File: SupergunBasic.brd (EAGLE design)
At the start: 114.9 x 67.3 mm, 33 parts, among them J1 AUDIO_JACK_3.5MM_PTH

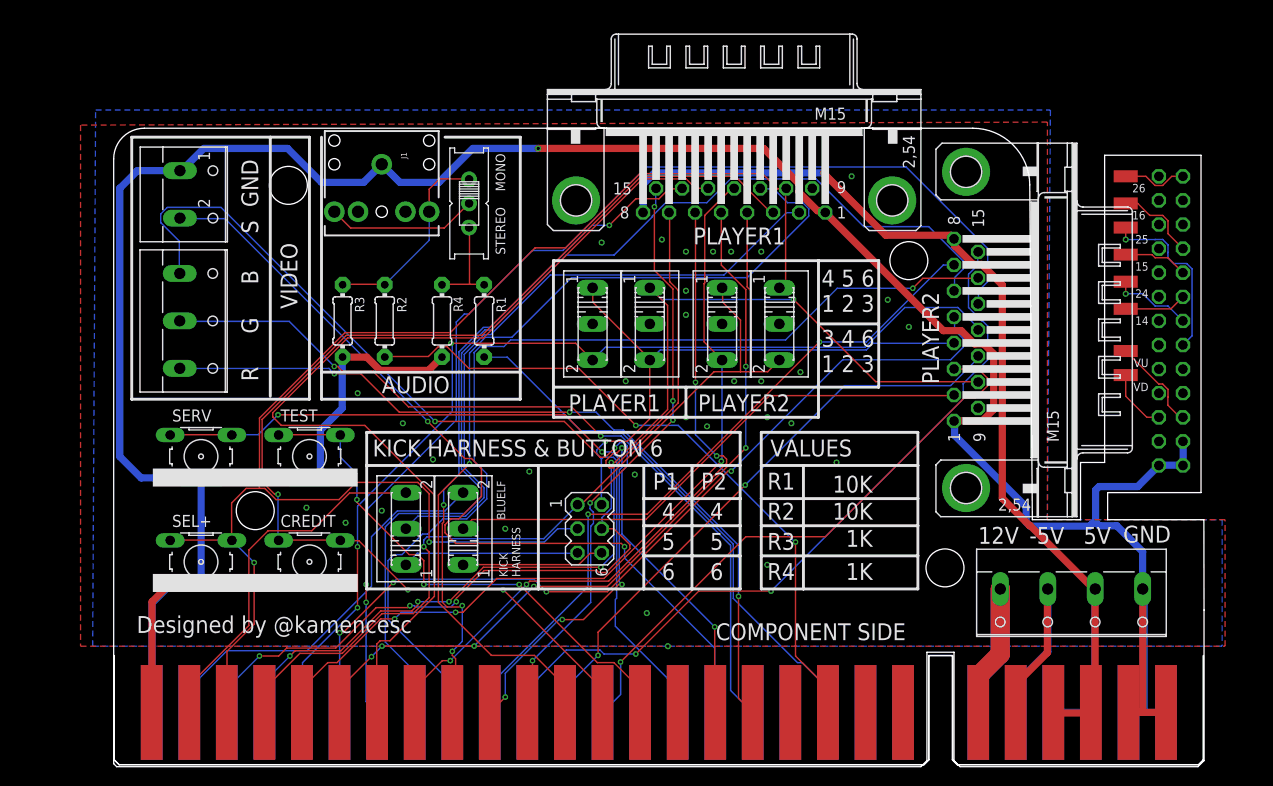
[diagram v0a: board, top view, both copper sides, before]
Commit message: Add files via upload
He estado trabajando en la versión con Scart, es mas fácil quitar que añadir cosas, así que en el momento de subir esta versión, es identica a la Scart pero sin los requisitos de este.
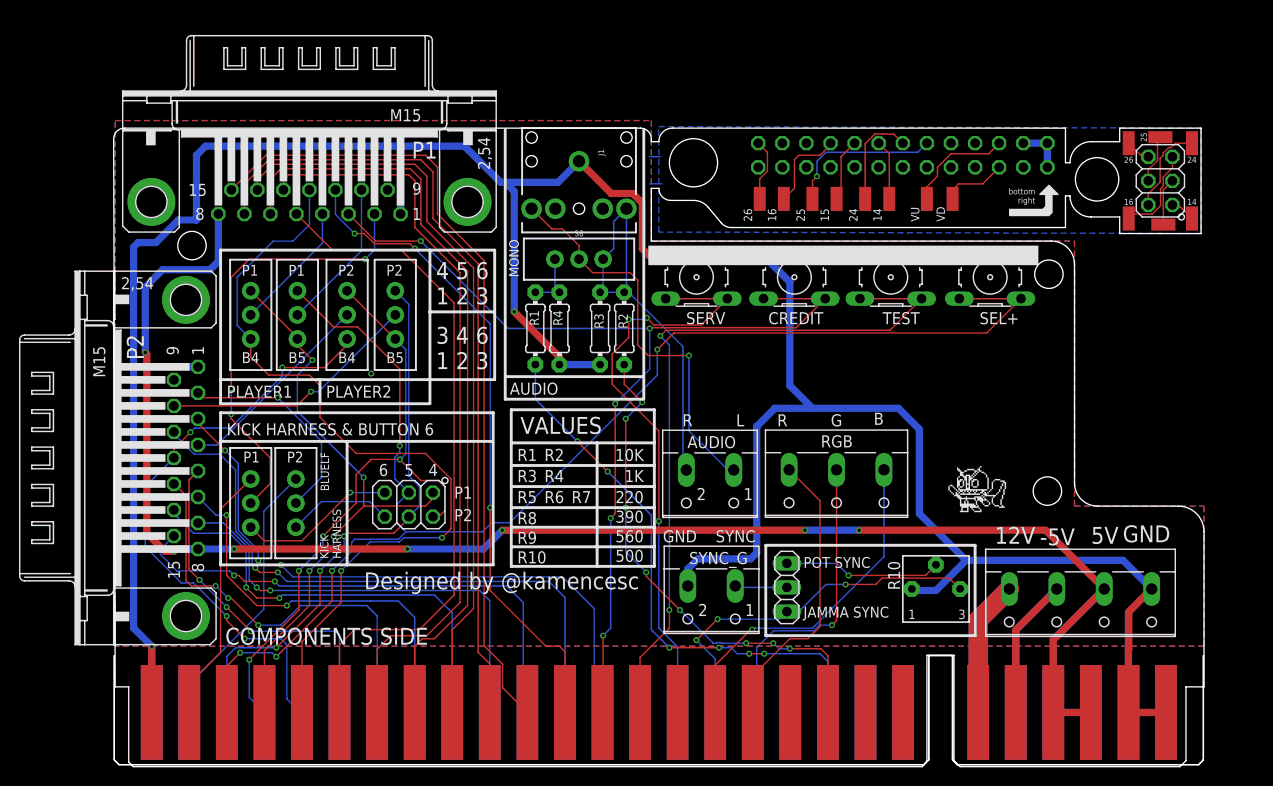
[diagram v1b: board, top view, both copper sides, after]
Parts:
- removed KH_CPS2: (no value), con-lstb:MA03-2
- removed MO_ST: (no value), adafruit:EG1218
- removed S2, S3, S5, S6: (no value), switch:255SB
- removed X4: (no value), con-wago-500:W237-102
- removed X5: (no value), con-wago-500:W237-103
- added 1, 2, 3, 4, 5, 6: (no value), wirepad:SMD1,27-2,54
- added AUDIO, SYNC_G: (no value), con-wago-500:W237-102
- added JP2, JP3: (no value), pinhead:2X03
- added JP4: (no value), pinhead:1X03
- added R10: (no value), bourns:3362P
- added RGB: (no value), con-wago-500:W237-103
- added S10, S11, S12, S8, S9: (no value), SparkFun-Switches:SWITCH_SPDT_PTH_11.6X4.0MM
- R1, R2: value (none) -> 10K
- R3, R4: value (none) -> 1K
- S1, S4: device switch:255SB -> SparkFun-Switches:SWITCH_SPDT_PTH_11.6X4.0MM
- moved SEL+ 88.4 mm to (92.4, 51.6), turned to 180 degrees
- moved PLAYER_2 83.3 mm to (7.62, 32.5), turned to 270 degrees
- moved TEST 64.1 mm to (81.9, 51.6), turned to 180 degrees
- moved CREDIT 59.3 mm to (71.8, 51.6), turned to 180 degrees
- moved SERV 55.5 mm to (61.4, 51.6), turned to 180 degrees
- moved S4 54.3 mm to (19.2, 27.8), turned to 180 degrees
- moved S1 53.2 mm to (14.4, 27.8), turned to 180 degrees
- moved PLAYER_1 44.8 mm to (20.6, 59.5)
- moved 26 38.6 mm to (68.1, 59.8), turned to 0 degrees
- moved 16 36.0 mm to (70.6, 59.8), turned to 0 degrees
- moved JP1 33.2 mm to (83.2, 64.5), turned to 180 degrees
- moved 25 33.2 mm to (73.7, 59.8), turned to 0 degrees
- moved 15 31.0 mm to (76.2, 59.8), turned to 0 degrees
- moved 24 28.8 mm to (79.2, 59.8), turned to 0 degrees
- moved 14 27.5 mm to (81.8, 59.8), turned to 0 degrees
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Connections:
- removed net N$11: JAMMA1.11
- removed net N$3: MO_ST.S, R1.1, R4.2
- removed net N$5: JAMMA2.M
- removed net P1_B6: PLAYER_1.2, S2.2
- removed net P2_B6: PLAYER_2.2, S3.2
- new net DIRECT_SYNC: JP4.2, SYNC_G.1
- new net K_14: 1.1, JP2.1
- new net K_15: 2.1, JP2.3
- new net K_16: 3.1, JP2.5
- new net K_24: 6.1, JP2.2
- new net K_25: 5.1, JP2.4
- new net K_26: 4.1, JP2.6
- new net P_SYNC: JP4.3, R10.2
- new net STR_LEFT: R1.1, R4.2, S8.3
- new net SW1_B6: PLAYER_1.2, S1.2
- new net SW2_B6: PLAYER_2.2, S4.2
- net AUDIO_LEFT: now also AUDIO.1, S8.2; no longer MO_ST.P
- net AUDIO_RIGHT: now also AUDIO.2, S8.1; no longer MO_ST.O
- net GND: now also R10.1, SYNC_G.2; no longer X4.1
- net J_BLUE: now also RGB.1; no longer X5.1
- net J_GREEN: now also RGB.2; no longer X5.2
- net J_P1_B6: now also S1.3; no longer S2.3
- net J_P2_B6: now also S4.3; no longer S3.3
- net J_RED: now also RGB.3; no longer X5.3
- net J_SYNC: now also JP4.1, R10.3; no longer X4.2
- net K_P1_B6: now also JP3.5, S1.1; no longer KH_CPS2.5, S2.1
- net K_P2_B6: now also JP3.6, S4.1; no longer KH_CPS2.6, S3.1
- net P1_B3: now also S9.3; no longer S1.3
- net P1_B4: now also JP3.1, S12.3, S9.1; no longer KH_CPS2.1, PLAYER_1.4, S1.1, S4.3
- net P1_B5: now also JP3.3, S12.1; no longer KH_CPS2.3, PLAYER_1.10, S4.1
- net P2_B3: now also S11.3; no longer S5.3
- net P2_B4: now also JP3.2, S10.3, S11.1; no longer KH_CPS2.2, PLAYER_2.4, S5.1, S6.3
- net P2_B5: now also JP3.4, S10.1; no longer KH_CPS2.4, PLAYER_2.10, S6.1
- net SW1_B4: now also PLAYER_1.4, S9.2; no longer S1.2
- net SW1_B5: now also PLAYER_1.10, S12.2; no longer S4.2
- net SW2_B4: now also PLAYER_2.4, S11.2; no longer S5.2
- net SW2_B5: now also PLAYER_2.10, S10.2; no longer S6.2
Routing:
- net P2_B1: track 118.2 -> 44.3 mm, vias 2 -> 3
- net P2_RIGHT: track 116.0 -> 42.2 mm, vias 0 -> 2
- net P1_B6: track 67.1 -> 0.00 mm
- net VCC: track 117.1 -> 183.4 mm, vias 1 -> 7
- net P2_B5: track 123.7 -> 59.3 mm, vias 5 -> 3
- net J_BLUE: track 100.7 -> 36.7 mm, vias 3 -> 1
- net P2_B6: track 57.6 -> 0.00 mm
- net P2_LEFT: track 104.3 -> 47.1 mm, vias 1 -> 2
- net J_GREEN: track 86.5 -> 32.5 mm, vias 2 -> 1
- net J_RED: track 84.9 -> 31.0 mm, vias 3 -> 0
- net P2_B2: track 91.3 -> 37.6 mm, vias 4 -> 3
- net P2_B4: track 119.8 -> 66.3 mm, vias 5 -> 4
- net J_SYNC: track 92.6 -> 39.4 mm, vias 2 -> 3
- net SW1_B6: track 0.00 -> 46.5 mm, vias 0 -> 3
- net P2_B3: track 105.3 -> 62.9 mm, vias 3 -> 4
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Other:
- outline, holes or cut-outs redrawn
- board text added: "14"
- board text added: "15"
- board text added: "16"
- board text added: "220"
- board text added: "24"
- board text added: "25"
- board text added: "26"
- board text added: "390"
- board text added: "500"
- board text added: "560"
- board text added: "B"
- board text added: "B4"
- board text added: "B5"
- board text added: "Basic Supergun + Scart V0.2"
- board text added: "COMPONENTS SIDE"
- board text added: "Faces to the PCB"
- board text added: "G"
- board text added: "JAMMA SYNC"
- board text added: "L"
- board text added: "POT SYNC"
- board text added: "R"
- board text added: "R10"
- board text added: "R5"
- board text added: "R6"
- board text added: "R7"
- board text added: "R8"
- board text added: "R9"
- board text added: "SYNC"
- board text added: "bottom right"
- board text removed: "Basic Supergun"
- board text removed: "COMPONENT SIDE"
- board text removed: "R G B"
- board text removed: "S GND"
- board text removed: "STEREO"
- board text removed: "VIDEO"

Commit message: Add files via upload
There ara some changesr since las versión, now there's a lm1881 sync stripper to get Sync On Green to Scart Connector. But if you are using a OSSC theres a switch to select Jamma Sync (original) or Csync (LM1881)

Now there's a LED to bring light to the PCB!

Minir improvements on design
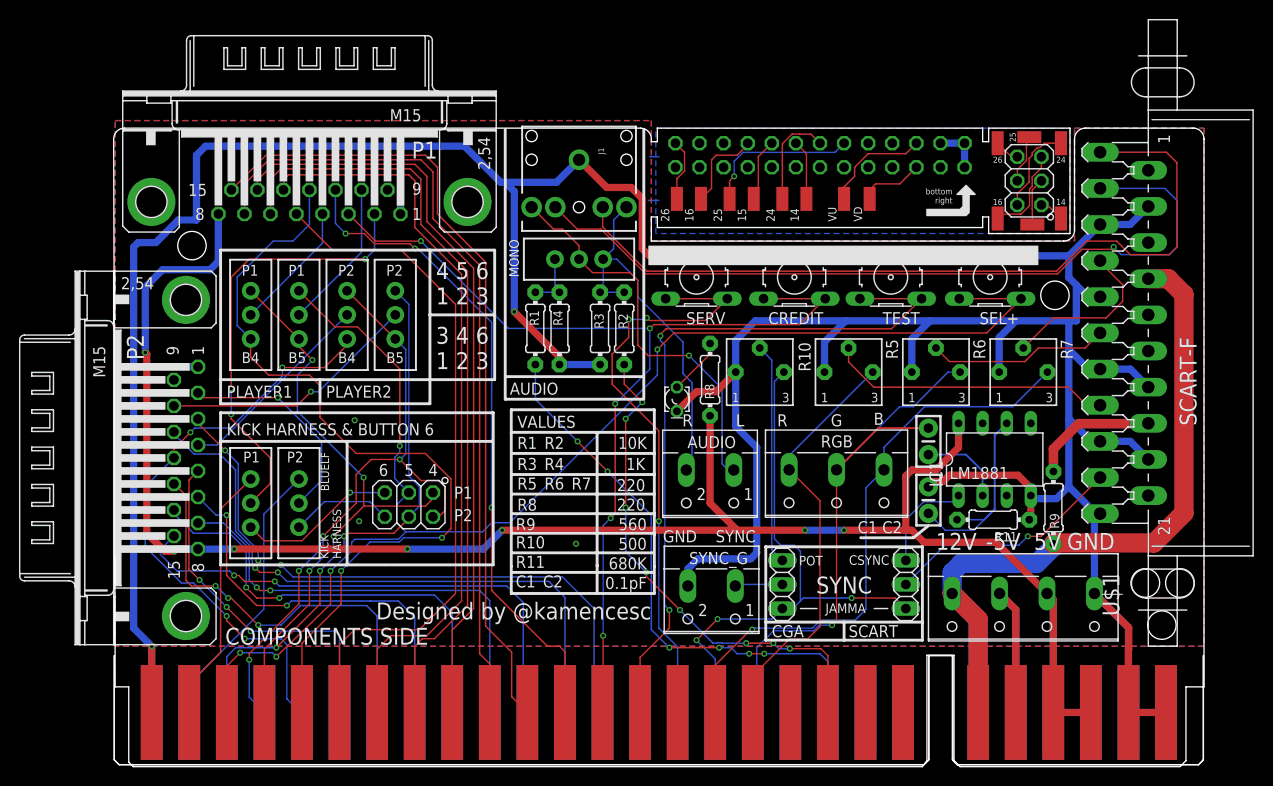
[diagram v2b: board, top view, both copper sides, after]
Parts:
- added C1, C2: 0.1uF, SparkFun-Capacitors:CAP-PTH-SMALL-KIT
- added IC1: LM1881N, oldchips2:DIL08
- added JP5: (no value), pinhead:1X03
- added LED1: (no value), led:LD260
- added R11: 680k, adafruit:0204/7
- added R5, R6, R7: (no value), bourns:3362P
- added R8: 220, adafruit:0204/7
- added R9: 560, adafruit:0204/7
- added U$1: SCART_F, scart:SCART_F
- moved R10 29.5 mm to (68.1, 41.6)
- moved 1 13.8 mm to (99.9, 57.8)
- moved 2 13.8 mm to (96.8, 57.1)
- moved 3 13.8 mm to (93.2, 57.8)
- moved 4 13.8 mm to (93.2, 65.7)
- moved 5 13.8 mm to (96.5, 66.4)
- moved 6 13.8 mm to (99.9, 65.7)
- moved JP2 13.8 mm to (96.5, 61.8)
- moved 15 8.73 mm to (67.5, 59.8)
- moved 24 8.73 mm to (70.5, 59.8)
- moved 25 8.73 mm to (64.9, 59.8)
- moved 26 8.73 mm to (59.4, 59.8)
- moved JP1 8.73 mm to (74.5, 64.5)
- moved VD 8.73 mm to (79.7, 59.8)
- moved 16 8.73 mm to (61.9, 59.8)
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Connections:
- new net A_LEFT_OUT: J1.TSH, U$1.3
- new net A_RIGHT_OUT: J1.RSH, U$1.1
- new net C_SYNC: IC1.1, JP5.3
- new net N$2: LED1.A, R8.2
- new net N$4: C2.1, IC1.6, R11.2
- new net N$5: C1.2, IC1.2
- new net SCART_FAST_SW: R9.2, U$1.16
- new net SCART_SYNC: JP5.2, U$1.19
- new net S_BLUE: R7.2, U$1.7
- new net S_GREEN: R6.2, U$1.11
- new net S_RED: R5.2, U$1.15
- new net VSYNC: IC1.3
- net GND: now also C2.2, IC1.4, LED1.K, R11.1, R5.1, R6.1, R7.1, U$1.13, U$1.14, U$1.17, U$1.18, U$1.21, U$1.4, U$1.5, U$1.9
- net J_BLUE: now also R7.3
- net J_GREEN: now also C1.1, R6.3
- net J_RED: now also R5.3
- net J_SYNC: now also JP5.1
- net VCC: now also IC1.8, R8.1
- net VCC+12: now also R9.1, U$1.8
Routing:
- net GND: track 355.4 -> 444.4 mm, vias 3 -> 5
- net A_RIGHT_OUT: track 0.00 -> 84.2 mm
- net A_LEFT_OUT: track 0.00 -> 83.8 mm, vias 0 -> 1
- net VCC+12: track 28.8 -> 84.3 mm
- net S_RED: track 0.00 -> 29.9 mm
- net J_GREEN: track 32.5 -> 61.3 mm
- net SCART_SYNC: track 0.00 -> 25.1 mm, vias 0 -> 1
- net J_BLUE: track 36.7 -> 61.7 mm
- net N$4: track 0.00 -> 21.0 mm
- net J_SYNC: track 39.4 -> 59.3 mm
- net S_GREEN: track 0.00 -> 19.1 mm
- net S_BLUE: track 0.00 -> 17.8 mm
- net VCC: track 183.4 -> 201.1 mm
- net J_RED: track 31.0 -> 44.9 mm
- net SCART_FAST_SW: track 0.00 -> 13.5 mm
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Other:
- outline, holes or cut-outs redrawn
- board text added: "0.1pF"
- board text added: "680K"
- board text added: "C1"
- board text added: "C1 C2"
- board text added: "C2"
- board text added: "CGA"
- board text added: "CSYNC"
- board text added: "JAMMA"
- board text added: "LM1881"
- board text added: "POT"
- board text added: "R11"
- board text added: "SCART"
- board text removed: "390"
- board text removed: "JAMMA SYNC"
- board text removed: "POT SYNC"
